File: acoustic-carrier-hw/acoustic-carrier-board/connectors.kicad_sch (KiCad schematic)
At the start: 1 part, among them J901 Conn_02x06_Odd_Even

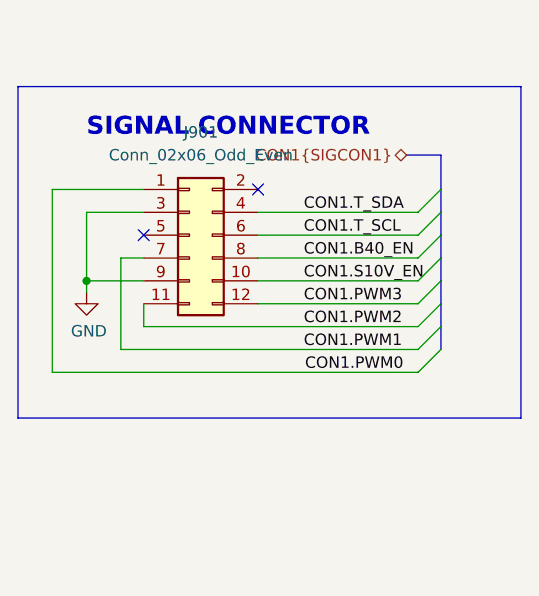
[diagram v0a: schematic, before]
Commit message: Did big ig parts of routing (next) make sure to re-add pull-ups/downs accordingly
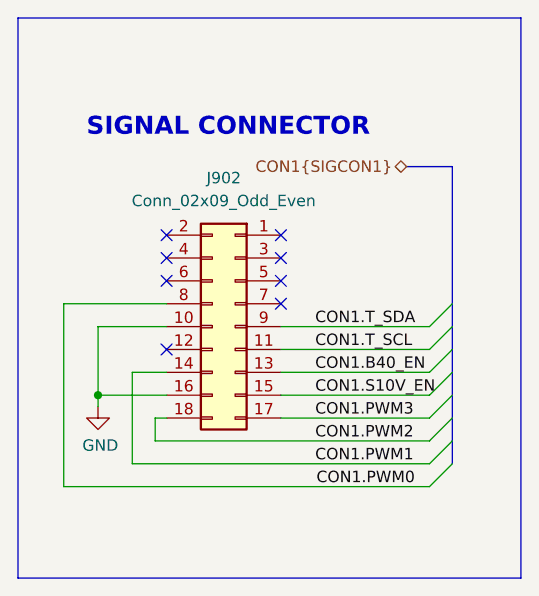
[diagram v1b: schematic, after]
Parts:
- removed J901: Conn_02x06_Odd_Even, Connector_PinSocket_2.54mm:PinSocket_2x06_P2.54mm_Horizontal, symbol Connector_Generic:Conn_02x06_Odd_Even
- added J902: Conn_02x09_Odd_Even, Connector_PinSocket_2.54mm:PinSocket_2x09_P2.54mm_Vertical, symbol Connector_Generic:Conn_02x09_Odd_Even
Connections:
- net CON1.B40_EN: now also J902.13 (Pin_13)
- net CON1.PWM0: now also J902.8 (Pin_8)
- net CON1.PWM1: now also J902.14 (Pin_14)
- net CON1.PWM2: now also J902.18 (Pin_18)
- net CON1.PWM3: now also J902.17 (Pin_17)
- net CON1.S10V_EN: now also J902.15 (Pin_15)
- net CON1.T_SCL: now also J902.11 (Pin_11)
- net CON1.T_SDA: now also J902.9 (Pin_9)
- net GND: now also J902.10 (Pin_10), J902.16 (Pin_16)
- no-connect marks 2 -> 8

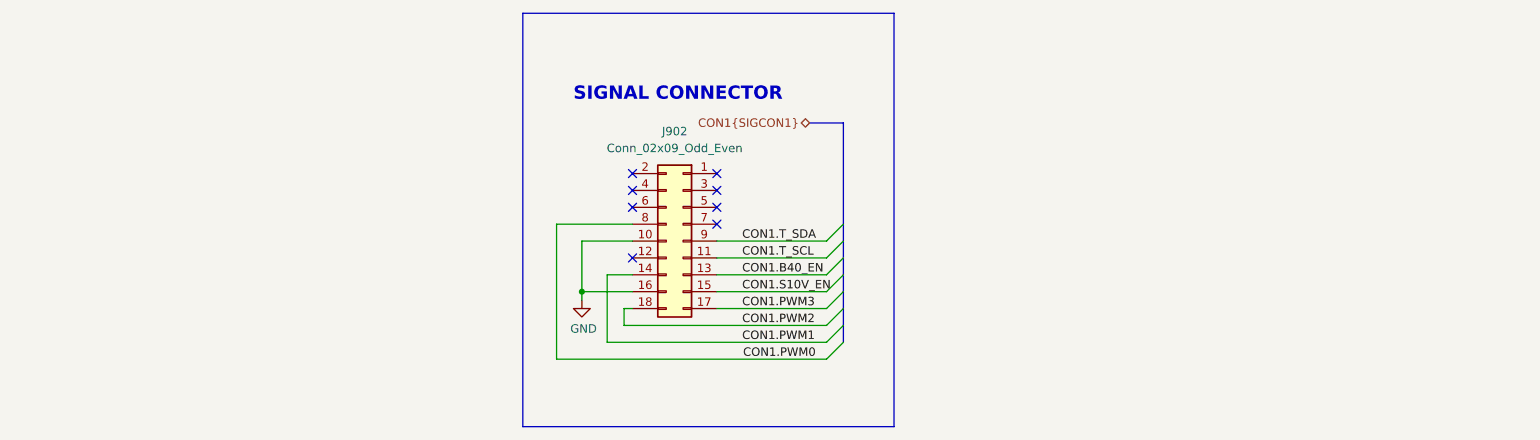
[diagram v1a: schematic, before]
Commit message: [carrier] Routed 6x2 IO connector
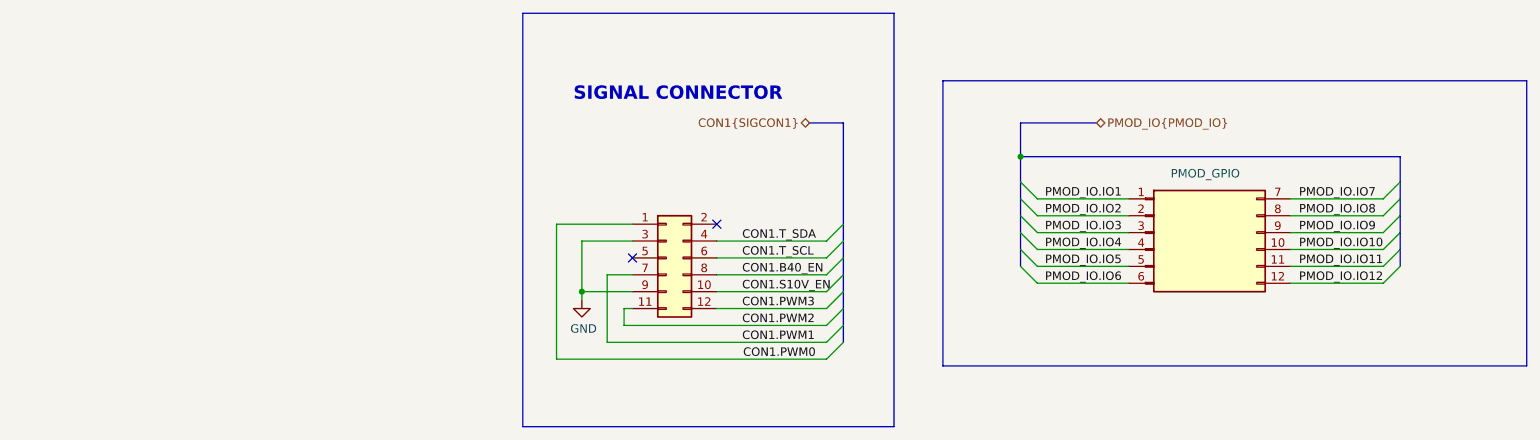
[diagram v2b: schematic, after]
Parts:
- removed J902: Conn_02x09_Odd_Even, Connector_PinSocket_2.54mm:PinSocket_2x09_P2.54mm_Vertical, symbol Connector_Generic:Conn_02x09_Odd_Even
- added J704: PMOD_GPIO, iw-connector:PMOD_Pinsocket, symbol iw-connector:PMOD_GPIO
- added J901: Conn_02x06_Odd_Even, symbol Connector_Generic:Conn_02x06_Odd_Even
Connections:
- net CON1.B40_EN: now also J901.8 (Pin_8)
- net CON1.PWM0: now also J901.1 (Pin_1)
- net CON1.PWM1: now also J901.7 (Pin_7)
- net CON1.PWM2: now also J901.11 (Pin_11)
- net CON1.PWM3: now also J901.12 (Pin_12)
- net CON1.S10V_EN: now also J901.10 (Pin_10)
- net CON1.T_SCL: now also J901.6 (Pin_6)
- net CON1.T_SDA: now also J901.4 (Pin_4)
- net GND: now also J901.3 (Pin_3), J901.9 (Pin_9)
- new net PMOD_IO.IO1: J704.1 (IO1/TMS)
- new net PMOD_IO.IO10: J704.10 (IO8)
- new net PMOD_IO.IO11: J704.11 (GND)
- new net PMOD_IO.IO12: J704.12 (Vcc)
- new net PMOD_IO.IO2: J704.2 (IO2/TDI)
- new net PMOD_IO.IO3: J704.3 (IO3/TDO)
- new net PMOD_IO.IO4: J704.4 (IO4/TCK)
- new net PMOD_IO.IO5: J704.5 (GND)
- new net PMOD_IO.IO6: J704.6 (Vcc)
- new net PMOD_IO.IO7: J704.7 (IO5)
- new net PMOD_IO.IO8: J704.8 (IO6)
- new net PMOD_IO.IO9: J704.9 (IO7)
- no-connect marks 8 -> 2

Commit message: [carrier] Routed out signals for board-to-board PTH
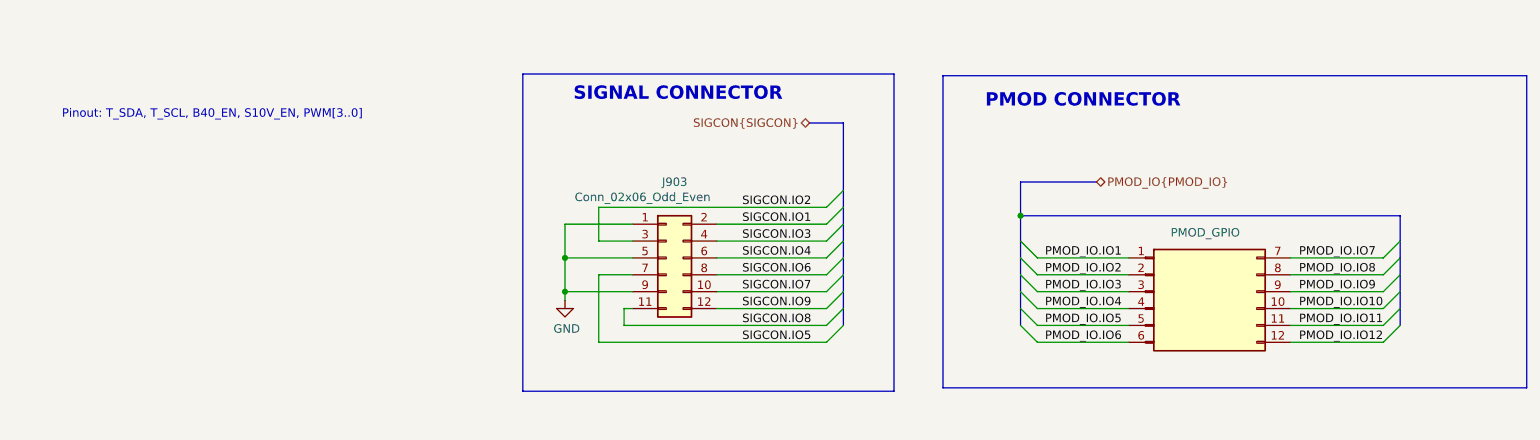
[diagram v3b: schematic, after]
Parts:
- removed J901: Conn_02x06_Odd_Even, symbol Connector_Generic:Conn_02x06_Odd_Even
- added J903: Conn_02x06_Odd_Even, Connector_PinSocket_2.54mm:PinSocket_2x06_P2.54mm_Vertical, symbol Connector_Generic:Conn_02x06_Odd_Even
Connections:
- net GND: now also J903.1 (Pin_1), J903.5 (Pin_5), J903.9 (Pin_9)
- new net SIGCON.IO1: J903.2 (Pin_2)
- new net SIGCON.IO2: J903.3 (Pin_3)
- new net SIGCON.IO3: J903.4 (Pin_4)
- new net SIGCON.IO4: J903.6 (Pin_6)
- new net SIGCON.IO5: J903.7 (Pin_7)
- new net SIGCON.IO6: J903.8 (Pin_8)
- new net SIGCON.IO7: J903.10 (Pin_10)
- new net SIGCON.IO8: J903.11 (Pin_11)
- new net SIGCON.IO9: J903.12 (Pin_12)
- no-connect marks 2 -> 0
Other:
- note added: "PMOD CONNECTOR"
- note added: "Pinout: T_SDA, T_SCL, B40_EN, S10V_EN, PWM[3..0]"
